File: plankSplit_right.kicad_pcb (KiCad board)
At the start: 2 copper layers, 113.2 x 119.2 mm, 84 parts, among them K1 XLR3, P1 USB_A, SW0:1 SPACE, SW0:2 ENTER, SW0:3 ALTGR, SW0:4 FN_R, SW0:5 MOD4, SW0:6 CTRL_R, SW1:1 B, SW1:2 M, SW1:3 ,, SW1:4 ., SW1:5 J, SW1:6 END, SW2:1 S, SW2:2 N, SW2:3 R, SW2:4 T, SW2:5 D, SW2:6 Y, SW3:1 K, SW3:2 H, SW3:3 G, SW3:4 F, SW3:5 Q, SW3:6 ẞ, SW4:1 6, SW4:2 7, SW4:3 8, SW4:4 9, SW4:5 0, SW4:6 BCKSPC, U1 ATmega32U4-AU, X1 CRYSTAL

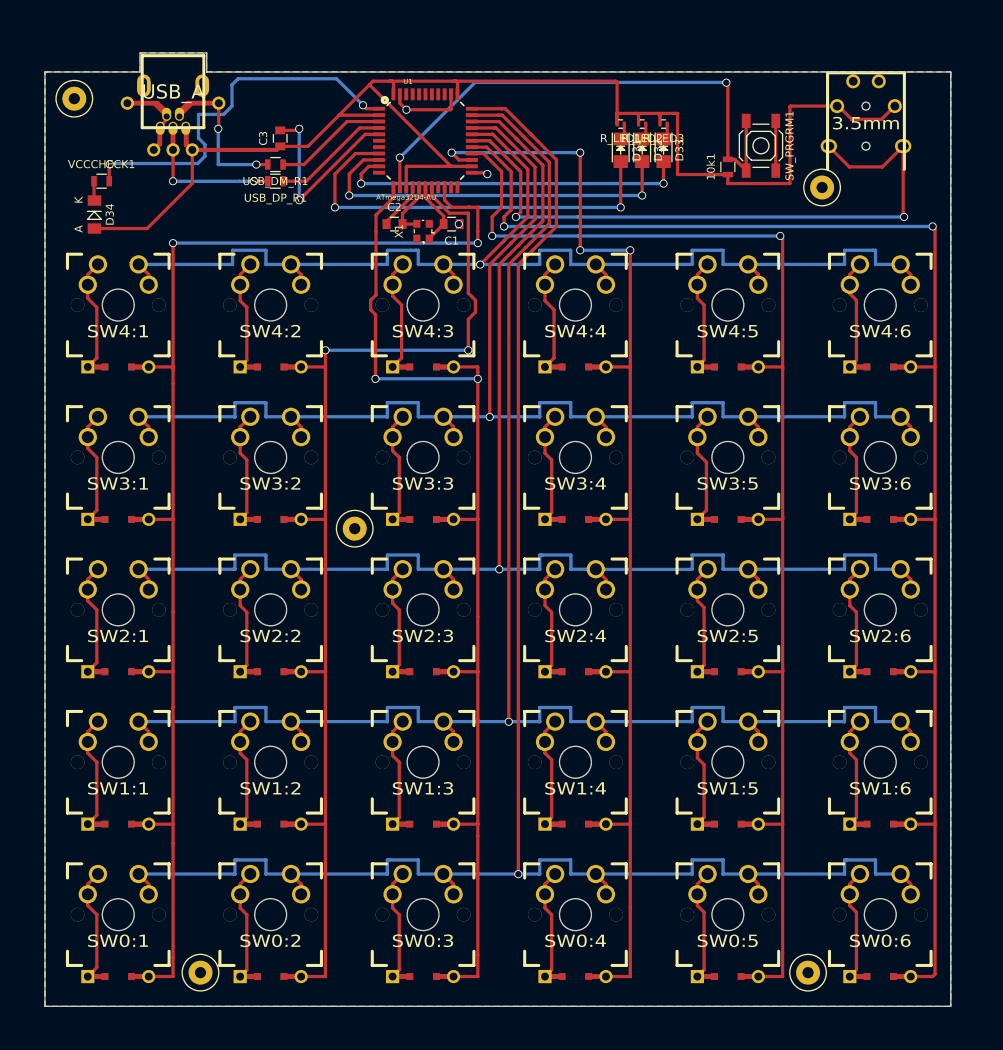
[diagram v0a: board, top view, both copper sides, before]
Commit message: added jtag and some capacitors
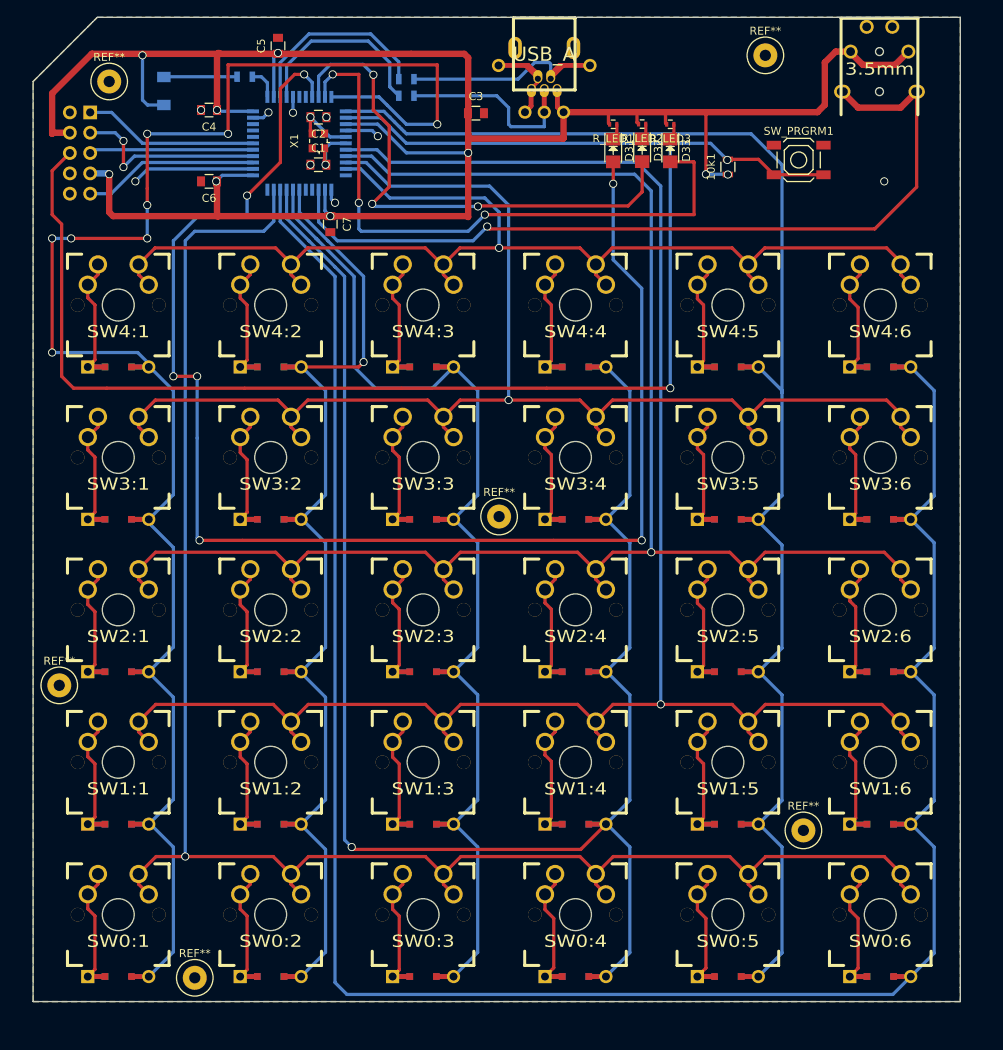
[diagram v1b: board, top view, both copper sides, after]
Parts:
- removed the REF** at (26.4, 22.7)
- removed the REF** at (118.1, 132.0)
- removed the REF** at (42.1, 132.0)
- removed the REF** at (61.4, 76.5)
- removed the REF** at (119.8, 33.8)
- added C4: C, Capacitors_SMD:C_0805, F.Cu at (43.2, 24.1)
- added C5: C, Capacitors_SMD:C_0805, F.Cu at (51.8, 16.1)
- added C6: C, Capacitors_SMD:C_0805, F.Cu at (43.2, 33.1)
- added C7: C, Capacitors_SMD:C_0805, F.Cu at (58.4, 38.4)
- added JTAG1: JTAG, aud:IDC_Header_Straight_10pins, B.Cu at (28.3, 24.4)
- added REF**: 1pin, Connect:1pin, F.Cu at (112.7, 17.3)
- added REF**: 1pin, Connect:1pin, F.Cu at (30.7, 20.6)
- added REF**: 1pin, Connect:1pin, F.Cu at (24.5, 96.1)
- added REF**: 1pin, Connect:1pin, F.Cu at (41.4, 132.6)
- added REF**: 1pin, Connect:1pin, F.Cu at (79.5, 75.0)
- added REF**: 1pin, Connect:1pin, F.Cu at (117.5, 114.2)
- D34, U1, USB_DM_R1, USB_DP_R1, VCCCHECK1: moved to B.Cu
- moved P1 46.6 mm to (85.1, 14.6)
- moved C3 24.7 mm to (76.6, 24.5), turned to 0 degrees
- moved VCCCHECK1 22.1 mm to (47.7, 20.0)
- moved USB_DP_R1 19.5 mm to (67.9, 22.4), turned to 0 degrees
- moved USB_DM_R1 19.5 mm to (67.9, 20.3), turned to 0 degrees
- moved C1 18.2 mm to (56.9, 31.0), turned to 0 degrees
- moved D34 17.7 mm to (37.6, 21.8)
- moved X1 17.3 mm to (56.9, 28.0)
- moved C2 16.4 mm to (56.9, 25.0), turned to 180 degrees
- moved U1 15.8 mm to (54.5, 28.3), turned to 270 degrees
- moved K1 7.02 mm to (127.0, 24.7)
- moved SW_PRGRM1 5.03 mm to (116.9, 30.4), turned to 0 degrees
- moved R_LED1 0.94 mm to (93.7, 25.9)
- moved D31 0.94 mm to (93.7, 29.2)
- moved R_LED3 0.84 mm to (100.9, 25.9)
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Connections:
- U1 pad 11: (no net) -> /COL0
- U1 pad 12: /COL2 -> /COL4
- U1 pad 18: /COL1 -> /ROW1
- U1 pad 19: (no net) -> /ROW2
- U1 pad 20: /COL0 -> /ROW3
- U1 pad 21: (no net) -> /ROW4
- U1 pad 25: /COL3 -> /DATA
- U1 pad 26: /COL4 -> (no net)
- U1 pad 27: /COL5 -> (no net)
- U1 pad 28: /DATA -> /COL1
- U1 pad 29: /ROW4 -> /COL2
- U1 pad 30: /ROW3 -> /COL3
- U1 pad 31: /ROW2 -> /COL5
- U1 pad 32: /ROW1 -> /ROW0
- U1 pad 33: /ROW0 -> (no net)
- U1 pad 36: (no net) -> /TDI
- U1 pad 37: (no net) -> /TDO
- U1 pad 38: (no net) -> /TMS
- U1 pad 39: (no net) -> /TCK
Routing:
- net /RST: track 67.1 -> 199.5 mm
- net /LED1: track 52.2 -> 179.8 mm, vias 2 -> 7
- net /P14_VCC: track 177.1 -> 280.0 mm, vias 0 -> 9
- net /COL5: track 177.1 -> 261.4 mm, vias 2 -> 0
- net /COL3: track 143.4 -> 205.0 mm, vias 4 -> 1
- net /COL0: track 156.1 -> 206.6 mm, vias 2 -> 8
- net /P1: track 47.5 -> 3.96 mm, vias 2 -> 0
- net /LED3: track 44.4 -> 78.2 mm, vias 2 -> 3
- net /TDO: track 0.00 -> 24.6 mm, vias 0 -> 2
- net /DATA: track 82.5 -> 105.7 mm, vias 2 -> 1
- net /TDI: track 0.00 -> 22.0 mm
- net /TCK: track 0.00 -> 22.0 mm
- net /UGND: track 59.3 -> 37.6 mm, vias 5 -> 8
- net /TMS: track 0.00 -> 20.5 mm
- net /ROW0: track 236.4 -> 215.9 mm
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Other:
- board size 113.2 x 119.2 mm -> 115.9 x 123 mm

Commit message: margin updated
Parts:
- moved REF** 23.5 mm to (136.2, 16.4)
- moved REF** 19.3 mm to (136.8, 113.9)
- moved REF** 2.69 mm to (41.1, 135.3)
- moved REF** 1.78 mm to (22.7, 96.1)
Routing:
- net (no net): vias 1 -> 14
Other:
- board size 115.9 x 123 mm -> 121.3 x 127.1 mm
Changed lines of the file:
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@@
     (links 219)
     (no_connects 2)
-    (area 21.130788 12.476754 137.18099 135.659276)
+    (area 19.065768 12.137295 140.47537 139.664856)
     (thickness 1.6)
-    (drawings 12)
-    (tracks 827)
+    (drawings 6)
+    (tracks 840)
     (zones 0)
     (modules 90)
@@
   )
   (module Connect:1pin (layer F.Cu)
-    (at 112.737229 17.306635)
+    (at 136.214449 16.415095)
     (descr "module 1 pin (ou trou mecanique de percage)")
     (tags DEV)
-    (fp_text reference REF** (at 0 -3.048) (layer F.SilkS)
+    (fp_text reference REF** (at 0 -3.048) (layer F.SilkS) hide
       (effects (font (size 1 1) (thickness 0.15)))
     )
-    (fp_text value 1pin (at 0 2.794) (layer F.Fab)
+    (fp_text value 1pin (at 0 2.794) (layer F.Fab) hide
       (effects (font (size 1 1) (thickness 0.15)))
     )
@@
     (descr "module 1 pin (ou trou mecanique de percage)")
     (tags DEV)
-    (fp_text reference REF** (at 0 -3.048) (layer F.SilkS)
+    (fp_text reference REF** (at 0 -3.048) (layer F.SilkS) hide
       (effects (font (size 1 1) (thickness 0.15)))
     )
-    (fp_text value 1pin (at 0 2.794) (layer F.Fab)
+    (fp_text value 1pin (at 0 2.794) (layer F.Fab) hide
       (effects (font (size 1 1) (thickness 0.15)))
     )
@@
   )
   (module Connect:1pin (layer F.Cu)
-    (at 24.474769 96.059335)
+    (at 22.691689 96.059335)
     (descr "module 1 pin (ou trou mecanique de percage)")
     (tags DEV)
-    (fp_text reference REF** (at 0 -3.048) (layer F.SilkS)
+    (fp_text reference REF** (at 0 -3.048) (layer F.SilkS) hide
       (effects (font (size 1 1) (thickness 0.15)))
     )
-    (fp_text value 1pin (at 0 2.794) (layer F.Fab)
+    (fp_text value 1pin (at 0 2.794) (layer F.Fab) hide
       (effects (font (size 1 1) (thickness 0.15)))
     )
@@
   )
   (module Connect:1pin (layer F.Cu)
-    (at 41.414029 132.612475)
+    (at 41.116849 135.287095)
     (descr "module 1 pin (ou trou mecanique de percage)")
     (tags DEV)
-    (fp_text reference REF** (at 0 -3.048) (layer F.SilkS)
+    (fp_text reference REF** (at 0 -3.048) (layer F.SilkS) hide
       (effects (font (size 1 1) (thickness 0.15)))
     )
-    (fp_text value 1pin (at 0 2.794) (layer F.Fab)
+    (fp_text value 1pin (at 0 2.794) (layer F.Fab) hide
       (effects (font (size 1 1) (thickness 0.15)))
     )
@@
     (descr "module 1 pin (ou trou mecanique de percage)")
     (tags DEV)
-    (fp_text reference REF** (at 0 -3.048) (layer F.SilkS)
+    (fp_text reference REF** (at 0 -3.048) (layer F.SilkS) hide
       (effects (font (size 1 1) (thickness 0.15)))
     )
-    (fp_text value 1pin (at 0 2.794) (layer F.Fab)
+    (fp_text value 1pin (at 0 2.794) (layer F.Fab) hide
       (effects (font (size 1 1) (thickness 0.15)))
     )
@@
   )
   (module Connect:1pin (layer F.Cu)
-    (at 117.492109 114.187315)
+    (at 136.808809 113.890135)
     (descr "module 1 pin (ou trou mecanique de percage)")
     (tags DEV)
-    (fp_text reference REF** (at 0 -3.048) (layer F.SilkS)
+    (fp_text reference REF** (at 0 -3.048) (layer F.SilkS) hide
       (effects (font (size 1 1) (thickness 0.15)))
     )
-    (fp_text value 1pin (at 0 2.794) (layer F.Fab)
+    (fp_text value 1pin (at 0 2.794) (layer F.Fab) hide
       (effects (font (size 1 1) (thickness 0.15)))
     )
@@
     (pad 1 thru_hole circle (at 0 0) (size 3 3) (drill 1.4) (layers *.Cu *.Mask F.SilkS))
   )
-  (gr_line (start 137.105989 12.551755) (end 135.917269 12.551755) (angle 90) (layer Edge.Cuts) (width 0.15))
-  (gr_line (start 137.105989 129.343495) (end 137.105989 12.551755) (angle 90) (layer Edge.Cuts) (width 0.15))
-  (gr_line (start 29.229649 12.551755) (end 135.917269 12.551755) (angle 90) (layer Edge.Cuts) (width 0.15))
-  (gr_line (start 28.635289 13.146115) (end 29.229649 12.551755) (angle 90) (layer Edge.Cuts) (width 0.15))
-  (gr_line (start 28.040929 13.740475) (end 28.635289 13.146115) (angle 90) (layer Edge.Cuts) (width 0.15))
-  (gr_line (start 21.205789 20.575615) (end 28.040929 13.740475) (angle 90) (layer Edge.Cuts) (width 0.15))
-  (gr_line (start 21.205789 135.584275) (end 21.205789 20.575615) (angle 90) (layer Edge.Cuts) (width 0.15))
-  (gr_line (start 21.800149 135.584275) (end 21.205789 135.584275) (angle 90) (layer Edge.Cuts) (width 0.15))
-  (gr_line (start 137.105989 135.584275) (end 21.800149 135.584275) (angle 90) (layer Edge.Cuts) (width 0.15))
-  (gr_line (start 137.105989 135.287095) (end 137.105989 135.584275) (angle 90) (layer Edge.Cuts) (width 0.15))
-  (gr_line (start 137.105989 133.801195) (end 137.105989 135.287095) (angle 90) (layer Edge.Cuts) (width 0.15))
-  (gr_line (start 137.105989 129.343495) (end 137.105989 133.801195) (angle 90) (layer Edge.Cuts) (width 0.15))
+  (gr_line (start 140.400369 12.462855) (end 140.400369 129.810855) (angle 90) (layer Edge.Cuts) (width 0.15))
+  (gr_line (start 28.919769 12.462855) (end 140.400369 12.462855) (angle 90) (layer Edge.Cuts) (width 0.15))
+  (gr_line (start 19.140769 22.241855) (end 28.919769 12.462855) (angle 90) (layer Edge.Cuts) (width 0.15))
+  (gr_line (start 19.140769 139.589855) (end 19.140769 22.241855) (angle 90) (layer Edge.Cuts) (width 0.15))
+  (gr_line (start 140.400369 139.589855) (end 19.140769 139.589855) (angle 90) (layer Edge.Cuts) (width 0.15))
+  (gr_line (start 140.400369 129.810855) (end 140.400369 139.589855) (angle 90) (layer Edge.Cuts) (width 0.15))
+  (via (at 79.750249 67.530055) (size 1.016) (drill 0.7874) (layers F.Cu B.Cu) (net 0))
+  (via (at 79.453069 113.592955) (size 1.016) (drill 0.7874) (layers F.Cu B.Cu) (net 0))
+  (via (at 98.472589 132.612475) (size 1.016) (drill 0.7874) (layers F.Cu B.Cu) (net 0))
+  (via (at 101.444389 77.039815) (size 1.016) (drill 0.7874) (layers F.Cu B.Cu) (net 0))
+  (via (at 76.481269 56.534395) (size 1.016) (drill 0.7874) (layers F.Cu B.Cu) (net 0))
   (via (at 127.596229 33.057175) (size 1.016) (drill 0.7874) (layers F.Cu B.Cu) (net 0))
+  (via (at 79.750249 132.909655) (size 1.016) (drill 0.7874) (layers F.Cu B.Cu) (net 0))
+  (via (at 110.656969 58.614655) (size 1.016) (drill 0.7874) (layers F.Cu B.Cu) (net 0))
+  (via (at 110.359789 96.653695) (size 1.016) (drill 0.7874) (layers F.Cu B.Cu) (net 0))
+  (via (at 117.194929 95.762155) (size 1.016) (drill 0.7874) (layers F.Cu B.Cu) (net 0))
+  (via (at 117.789289 76.148275) (size 1.016) (drill 0.7874) (layers F.Cu B.Cu) (net 0))
+  (via (at 117.492109 56.534395) (size 1.016) (drill 0.7874) (layers F.Cu B.Cu) (net 0))
+  (via (at 79.155889 48.213355) (size 1.016) (drill 0.7874) (layers F.Cu B.Cu) (net 0))
+  (via (at 79.155889 95.167795) (size 1.016) (drill 0.7874) (layers F.Cu B.Cu) (net 0))
   (segment (start 59.244829 40.486675) (end 76.184089 40.486675) (width 0.4064) (layer B.Cu) (net 1))
   (segment (start 56.889949 38.131795) (end 59.244829 40.486675) (width 0.4064) (layer B.Cu) (net 1))
@@
     (polygon
       (pts
-        (xy 137.105989 135.584275) (xy 21.205789 135.584275) (xy 21.205789 20.575615) (xy 29.229649 12.551755) (xy 137.105989 12.551755)
-        (xy 137.105989 135.584275)
+        (xy 140.382589 12.480635) (xy 28.919769 12.460315) (xy 19.150929 22.254555) (xy 19.168709 139.582235) (xy 140.390209 139.582235)
+        (xy 140.395289 12.470475)
       )
     )
@@
     (polygon
       (pts
-        (xy 137.105989 135.584275) (xy 21.205789 135.584275) (xy 21.205789 20.575615) (xy 29.229649 12.551755) (xy 137.105989 12.551755)
-        (xy 137.105989 135.584275)
+        (xy 140.405449 12.457775) (xy 28.924849 12.457775) (xy 19.140769 22.239315) (xy 19.145849 139.572075) (xy 140.405449 139.605095)
+        (xy 140.397829 12.480635)
       )
     )
